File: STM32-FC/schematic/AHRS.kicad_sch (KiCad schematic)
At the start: 16 parts, among them U5 ICM-45686, U6 ICM-45686, U7 BMM350, U8 ICP-20100, U9 BMP390

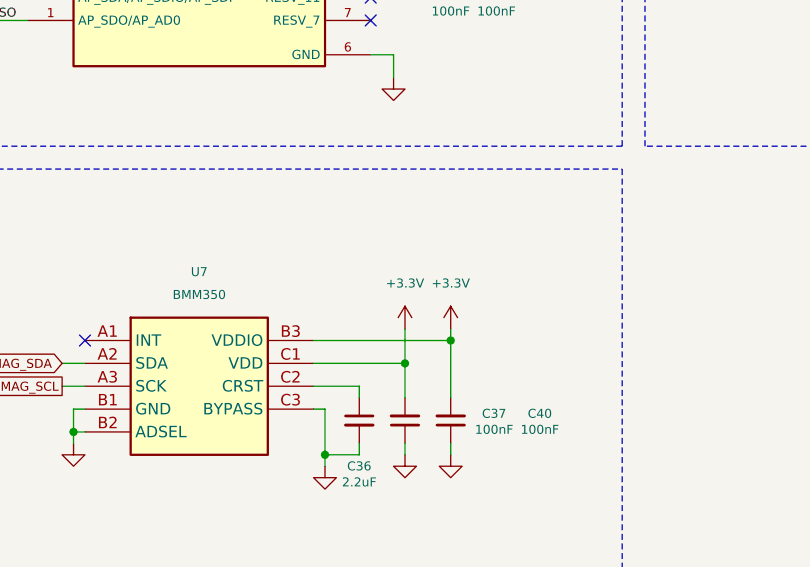
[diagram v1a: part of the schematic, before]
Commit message: fix : BMM350 power 1.8V and add dc2dc converter for 1.8V
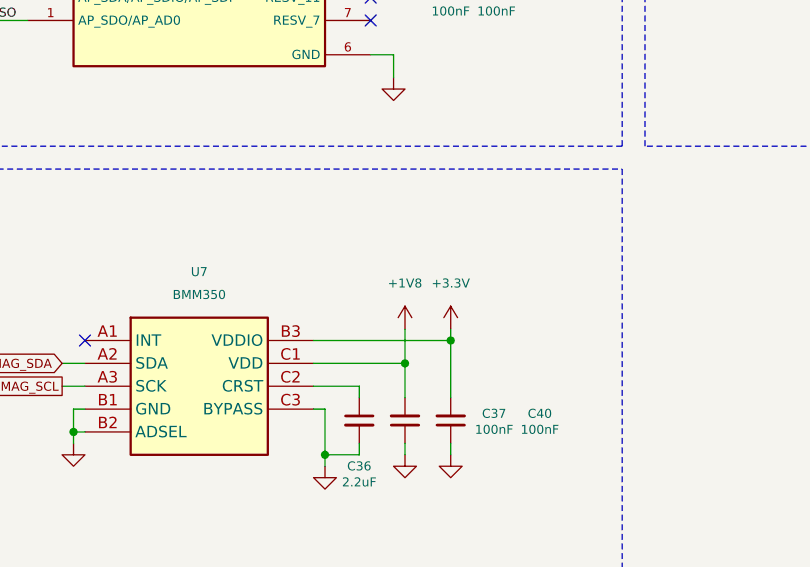
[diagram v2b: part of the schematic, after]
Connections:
- net +3.3V: no longer C37.2, U7.C1 (VDD)
- new net +1V8: C37.2, U7.C1 (VDD)

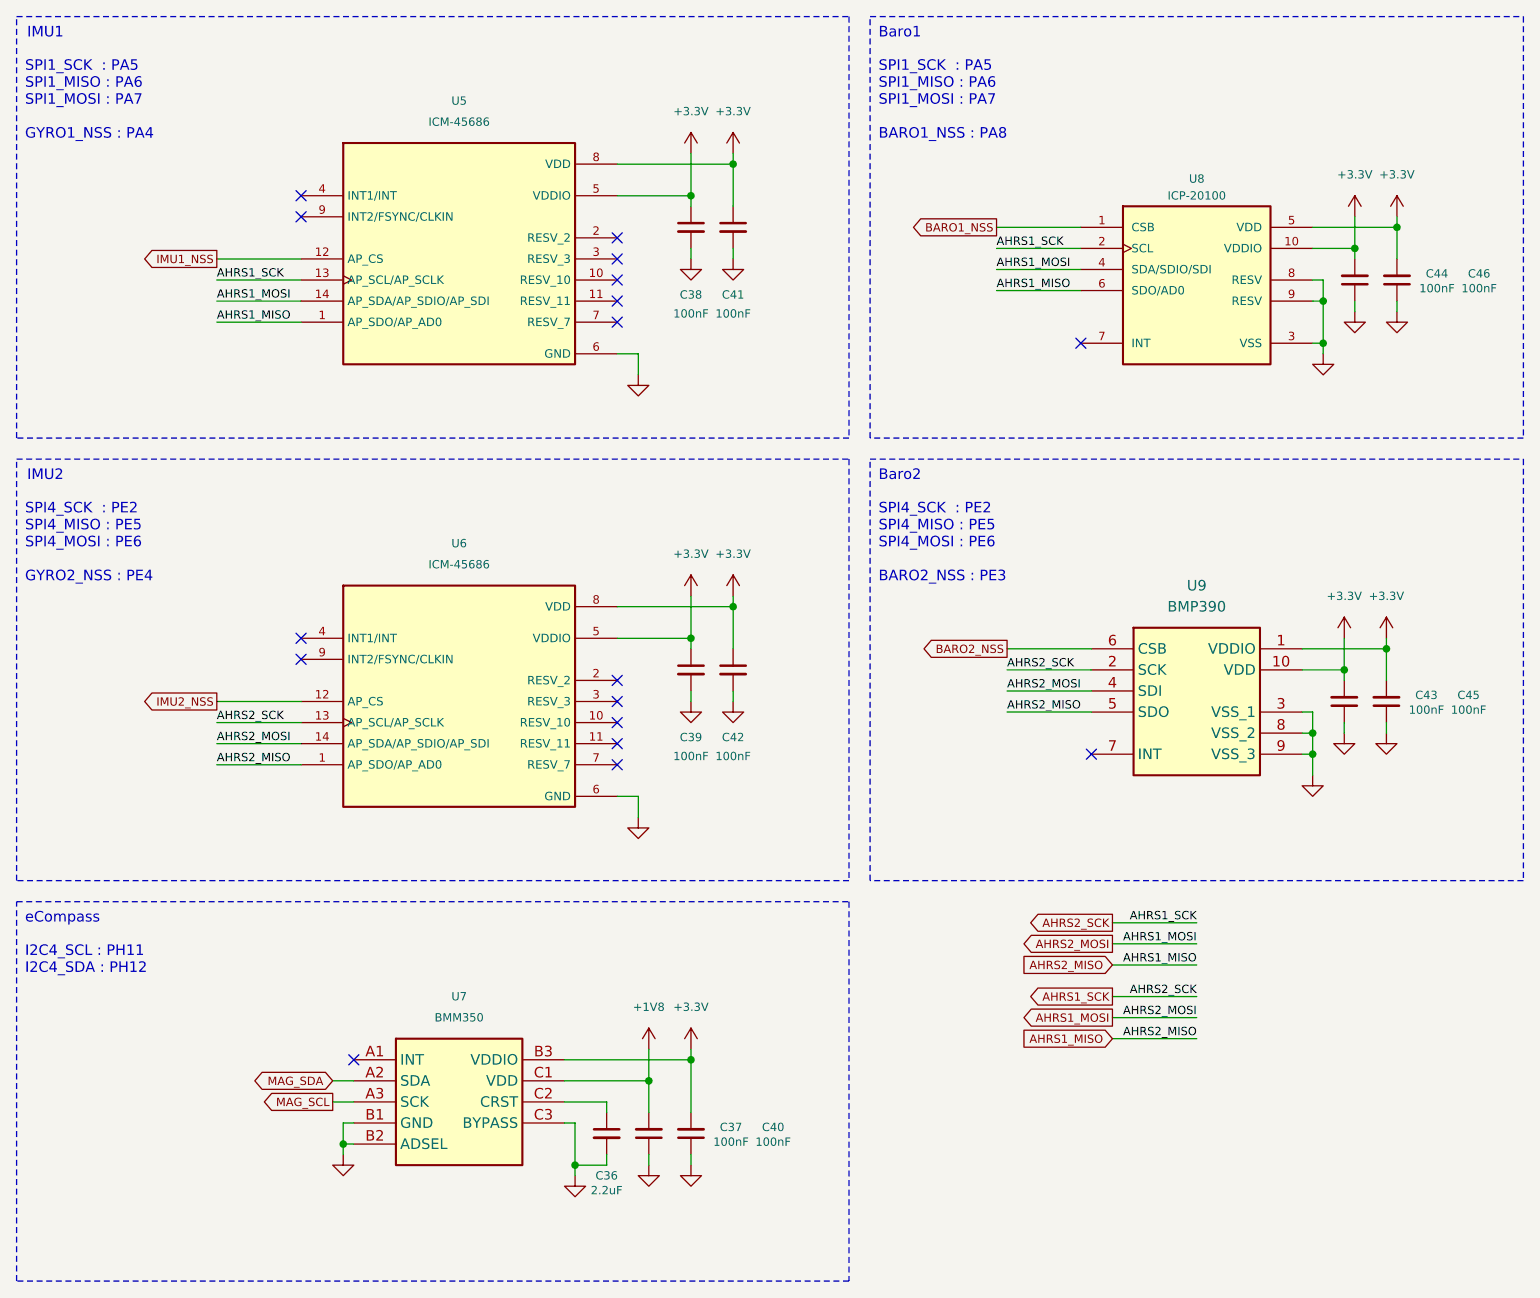
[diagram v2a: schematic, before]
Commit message: update : BOM and minor fix
- remove : DC2DC for analog
- change : JST SM conn. to BM
- change : ELRS conn. to JST XH (instead of JST SM)
- update : BOM List
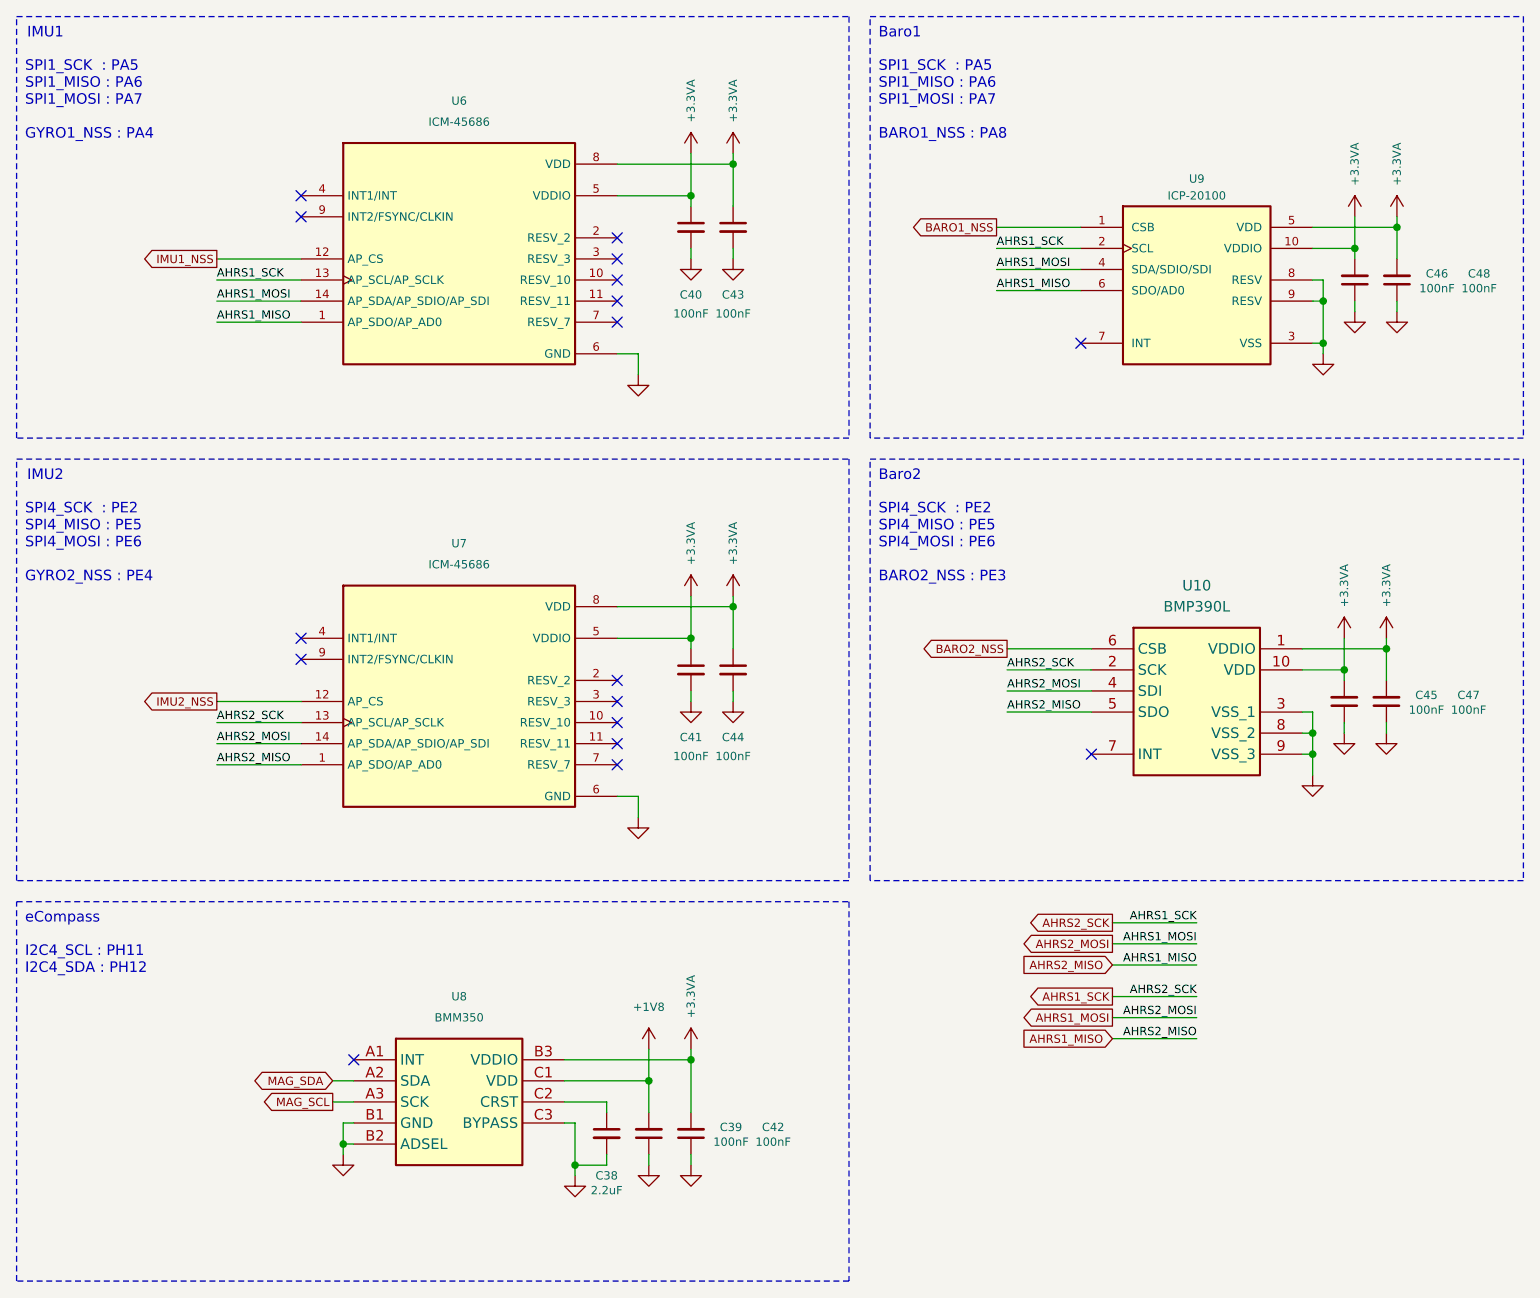
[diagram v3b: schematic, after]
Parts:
- C40: renamed from C38; LCSC C152819 -> C1525
- C41: renamed from C39; LCSC C152819 -> C1525
- C43: renamed from C41; LCSC C152819 -> C1525
- C44: renamed from C42; LCSC C152819 -> C1525
- U10: renamed from U9; value BMP390 -> BMP390L; LCSC (none) -> C2684802
- U6: renamed from U5; LCSC (none) -> C22459454
- U7: renamed from U6; LCSC (none) -> C22459454
- U8: renamed from U7; LCSC (none) -> C17225907
- U9: renamed from U8; LCSC (none) -> C5343527
- renumbered C36 to C38, C37 to C39, C40 to C42, C43 to C45, C44 to C46, C45 to C47, C46 to C48
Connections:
- net +3.3V renamed +3.3VA

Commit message: change : RC size 0402 to 0201
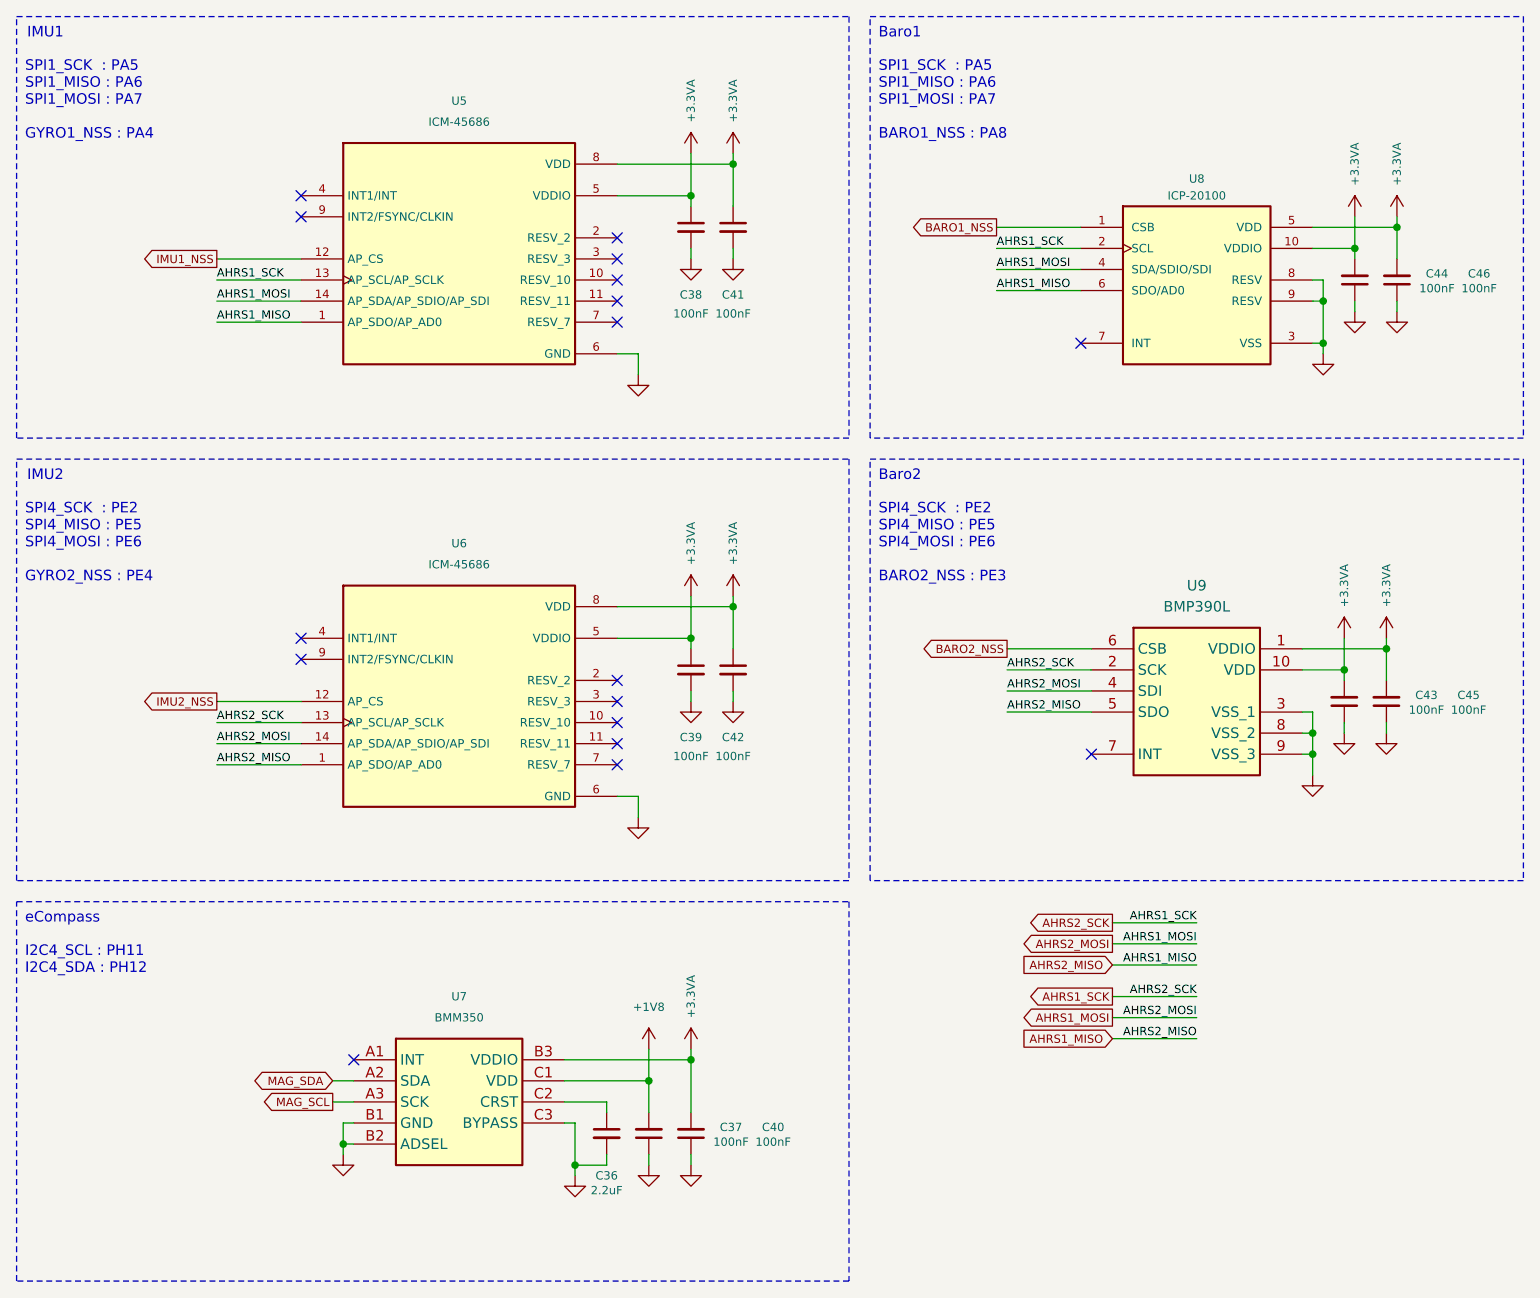
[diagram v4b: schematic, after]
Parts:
- C37: renamed from C39; footprint Capacitor_SMD:C_0402_1005Metric -> Capacitor_SMD:C_0201_0603Metric; LCSC C1525 -> C49062
- C38: renamed from C40; footprint Capacitor_SMD:C_0402_1005Metric -> Capacitor_SMD:C_0201_0603Metric; LCSC C1525 -> C49062
- C39: renamed from C41; footprint Capacitor_SMD:C_0402_1005Metric -> Capacitor_SMD:C_0201_0603Metric; LCSC C1525 -> C49062
- C40: renamed from C42; footprint Capacitor_SMD:C_0402_1005Metric -> Capacitor_SMD:C_0201_0603Metric; LCSC C1525 -> C49062
- C41: renamed from C43; footprint Capacitor_SMD:C_0402_1005Metric -> Capacitor_SMD:C_0201_0603Metric; LCSC C1525 -> C49062
- C42: renamed from C44; footprint Capacitor_SMD:C_0402_1005Metric -> Capacitor_SMD:C_0201_0603Metric; LCSC C1525 -> C49062
- C43: renamed from C45; footprint Capacitor_SMD:C_0402_1005Metric -> Capacitor_SMD:C_0201_0603Metric; LCSC C1525 -> C49062
- C44: renamed from C46; footprint Capacitor_SMD:C_0402_1005Metric -> Capacitor_SMD:C_0201_0603Metric; LCSC C1525 -> C49062
- C45: renamed from C47; footprint Capacitor_SMD:C_0402_1005Metric -> Capacitor_SMD:C_0201_0603Metric; LCSC C1525 -> C49062
- C46: renamed from C48; footprint Capacitor_SMD:C_0402_1005Metric -> Capacitor_SMD:C_0201_0603Metric; LCSC C1525 -> C49062
- renumbered C38 to C36, U6 to U5, U7 to U6, U8 to U7, U9 to U8, U10 to U9
